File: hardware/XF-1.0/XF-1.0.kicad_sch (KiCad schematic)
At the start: 9 parts

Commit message: modified:   Ferrite Transformer Calculation.xlsx 	modified:   README.md 	deleted:    hardware/XF-1.0/XF-1.0-backups/XF-1.0-2025-07-15_095716.zip 	new file:   hardware/XF-1.0/XF-1.0-backups/XF-1.0-2025-07-15_145509.zip 	new file:   hardware/XF-1.0/XF-1.0-backups/XF-1.0-2025-07-15_150114.zip 	new file:   hardware/XF-1.0/XF-1.0-backups/XF-1.0-2025-07-15_150614.zip 	new file:   hardware/XF-1.0/XF-1.0-backups/XF-1.0-2025-07-15_151503.zip 	new file:   hardware/XF-1.0/XF-1.0-backups/XF-1.0-2025-07-15_152320.zip 	new file:   hardware/XF-1.0/XF-1.0-backups/XF-1.0-2025-07-15_154638.zip 	modified:   hardware/XF-1.0/XF-1.0.kicad_pcb 	modified:   hardware/XF-1.0/XF-1.0.kicad_prl 	modified:   hardware/XF-1.0/XF-1.0.kicad_pro 	modified:   hardware/XF-1.0/XF-1.0.kicad_sch 	modified:   hardware/XF-1.0/_autosave-XF-1.0.kicad_sch 	modified:   hardware/XF-1.0/fp-info-cache
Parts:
- removed C1-2, C1-3: 1nF, Capacitor_THT:C_Rect_L13.0mm_W8.0mm_P10.00mm_FKS3_FKP3_MKS4, symbol Device:C
- removed L1, L2: ~, Transformer_THT:Inductor-EE25, symbol Device:L_Ferrite
- removed TF1: ~, Transformer_THT:EE35-1P-1S-Vertical-2143, symbol Transformer:ER35-1P-1S
- added CN1, CN2: Conn_01x02, Connector_Molex:Molex_KK-396_5273-03A_1x03_P3.96mm_Vertical_2, symbol Connector_Generic:Conn_01x02
- added L1, L2: 29µH, Inductor_THT:L_Radial_Multilayer_D8.0mm_P12.70mm, symbol Device:L
- added XF1: ~, Transformer_THT:Transformer_Toroid_Horizontal_OD40_ID23_H15, symbol Transformer:TRANSF1
- C1: renamed from C1-1; value 1nF -> 2.7nF
- R1: value R_US -> RBTL
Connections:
- net at C3.1: now also C1.2, L2.2
- net at C3.2, R1.2: now also CN2.2 (Pin_2)
- net at C1.1, C2.1: now also L1.2
- net at C2.2, R1.1: now also CN2.1 (Pin_1)
- new net: L1.1, XF1.4
- new net: L2.1, XF1.3
- new net: CN1.1 (Pin_1), XF1.1
- new net: CN1.2 (Pin_2), XF1.2
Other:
- moved on the sheet: C1

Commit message: modified:   Ferrite Transformer Calculation.xlsx 	modified:   README.md 	deleted:    hardware/CTL-1.0/CTL-1.0-backups/CTL-1.0-2025-05-28_203223.zip 	new file:   hardware/CTL-1.0/CTL-1.0-backups/CTL-1.0-2025-07-16_143147.zip 	deleted:    hardware/PS-2.0/PS-2.0-backups/PS-2.0-2025-05-06_105341.zip 	new file:   hardware/PS-2.0/PS-2.0-backups/PS-2.0-2025-07-17_090338.zip 	deleted:    hardware/XF-1.0/#auto_saved_files# 	deleted:    hardware/XF-1.0/XF-1.0-backups/XF-1.0-2025-07-15_145509.zip 	new file:   hardware/XF-1.0/XF-1.0-backups/XF-1.0-2025-07-16_140719.zip 	new file:   hardware/XF-1.0/XF-1.0-backups/XF-1.0-2025-07-17_091914.zip 	new file:   hardware/XF-1.0/XF-1.0-backups/XF-1.0-2025-07-17_092825.zip 	new file:   hardware/XF-1.0/XF-1.0-backups/XF-1.0-2025-07-17_093426.zip 	new file:   hardware/XF-1.0/XF-1.0-backups/XF-1.0-2025-07-17_103845.zip 	new file:   hardware/XF-1.0/XF-1.0-backups/XF-1.0-2025-07-17_105026.zip 	new file:   hardware/XF-1.0/XF-1.0-backups/XF-1.0-2025-07-17_105651.zip 	modified:   hardware/XF-1.0/XF-1.0.kicad_pcb 	modified:   hardware/XF-1.0/XF-1.0.kicad_pro 	modified:   hardware/XF-1.0/XF-1.0.kicad_sch 	deleted:    hardware/XF-1.0/_autosave-XF-1.0.kicad_sch 	modified:   hardware/XF-1.0/fp-info-cache 	modified:   log.md
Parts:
- added C1-1, C1-3, C4-1, C4-2, C4-3: 2.7nF, Capacitor_THT:C_Rect_L13.0mm_W8.0mm_P10.00mm_FKS3_FKP3_MKS4, symbol Device:C
- added C5, C6: 4.7nF, Capacitor_THT:C_Rect_L13.0mm_W8.0mm_P10.00mm_FKS3_FKP3_MKS4, symbol Device:C
- added CN3, CN4: Conn_01x02, Connector_Molex:Molex_KK-396_5273-03A_1x03_P3.96mm_Vertical_2, symbol Connector_Generic:Conn_01x02
- added H1, H2, H3, H4: ~, MountingHole:MountingHole_3mm_Pad, symbol Mechanical:MountingHole_Pad
- added L3, L4: 29µH, Inductor_THT:L_Radial_Multilayer_D8.0mm_P12.70mm, symbol Device:L
- added R2: RBTL, symbol Device:R_US
- added XF2: ~, Transformer_THT:Transformer_Toroid_Horizontal_OD40_ID23_H15, symbol Transformer:TRANSF1
- renumbered C1 to C1-2
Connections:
- net at C3.1, L2.2: now also C1-3.2; no longer C1-2.2
- net at C2.1, L1.2: now also C1-1.1; no longer C1-2.1
- new net: C5.2, CN4.1 (Pin_1), R2.1
- new net: C6.2, CN4.2 (Pin_2), R2.2
- new net: C1-1.2, C1-2.1
- new net: C1-2.2, C1-3.1
- new net: L4.1, XF2.3
- new net: C4-3.2, C6.1, L4.2
- new net: C4-1.1, C5.1, L3.2
- new net: C4-1.2, C4-2.1
- new net: C4-2.2, C4-3.1
- new net: L3.1, XF2.4
- new net: CN3.1 (Pin_1), XF2.1
- new net: CN3.2 (Pin_2), XF2.2

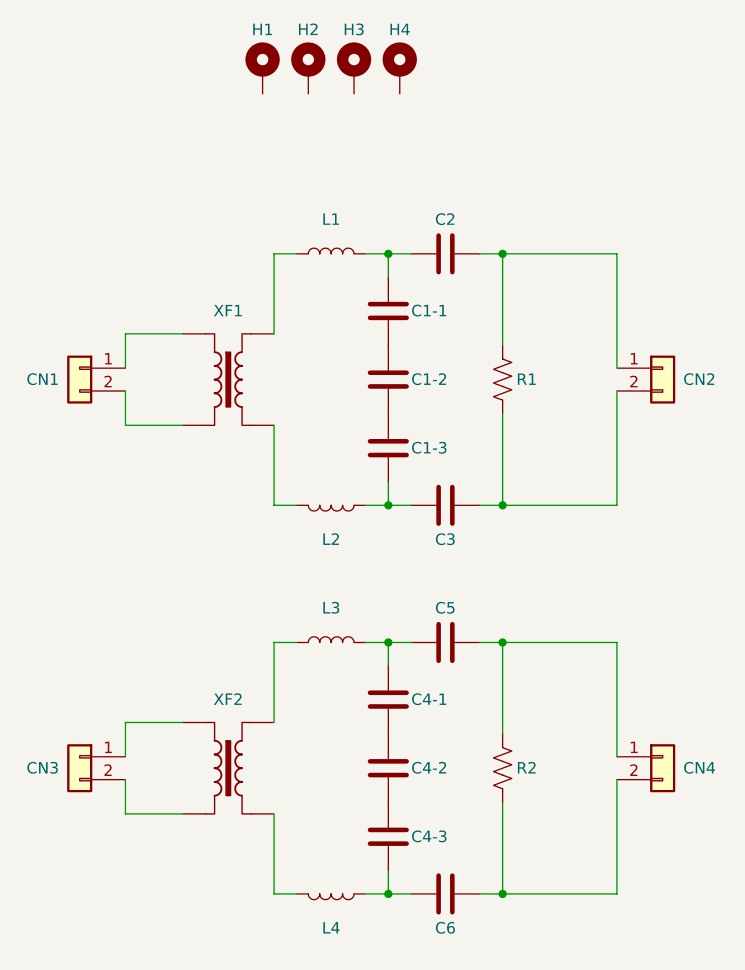
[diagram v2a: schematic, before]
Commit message: deleted:    hardware/PS-2.0/PS-2.0-backups/PS-2.0-2025-05-06_110321.zip 	deleted:    hardware/PS-2.0/PS-2.0-backups/PS-2.0-2025-05-06_111001.zip 	deleted:    hardware/PS-2.0/PS-2.0-backups/PS-2.0-2025-05-06_111519.zip 	deleted:    hardware/PS-2.0/PS-2.0-backups/PS-2.0-2025-05-06_112237.zip 	new file:   hardware/PS-2.0/PS-2.0-backups/PS-2.0-2025-07-17_141237.zip 	new file:   hardware/PS-2.0/PS-2.0-backups/PS-2.0-2025-07-17_142153.zip 	new file:   hardware/PS-2.0/PS-2.0-backups/PS-2.0-2025-07-17_143639.zip 	new file:   hardware/PS-2.0/PS-2.0-backups/PS-2.0-2025-07-17_144647.zip 	deleted:    hardware/XF-1.0/XF-1.0-backups/XF-1.0-2025-07-17_091914.zip 	deleted:    hardware/XF-1.0/XF-1.0-backups/XF-1.0-2025-07-17_092825.zip 	deleted:    hardware/XF-1.0/XF-1.0-backups/XF-1.0-2025-07-17_093426.zip 	deleted:    hardware/XF-1.0/XF-1.0-backups/XF-1.0-2025-07-17_103845.zip 	deleted:    hardware/XF-1.0/XF-1.0-backups/XF-1.0-2025-07-17_105026.zip 	deleted:    hardware/XF-1.0/XF-1.0-backups/XF-1.0-2025-07-17_105651.zip 	new file:   hardware/XF-1.0/XF-1.0-backups/XF-1.0-2025-07-17_144932.zip 	new file:   hardware/XF-1.0/XF-1.0-backups/XF-1.0-2025-07-17_145542.zip 	new file:   hardware/XF-1.0/XF-1.0-backups/XF-1.0-2025-07-17_150101.zip 	new file:   hardware/XF-1.0/XF-1.0-backups/XF-1.0-2025-07-17_150621.zip 	new file:   hardware/XF-1.0/XF-1.0-backups/XF-1.0-2025-07-17_151256.zip 	new file:   hardware/XF-1.0/XF-1.0-backups/XF-1.0-2025-07-17_151907.zip 	modified:   hardware/XF-1.0/XF-1.0.kicad_pcb 	modified:   hardware/XF-1.0/XF-1.0.kicad_pro 	modified:   hardware/XF-1.0/XF-1.0.kicad_sch
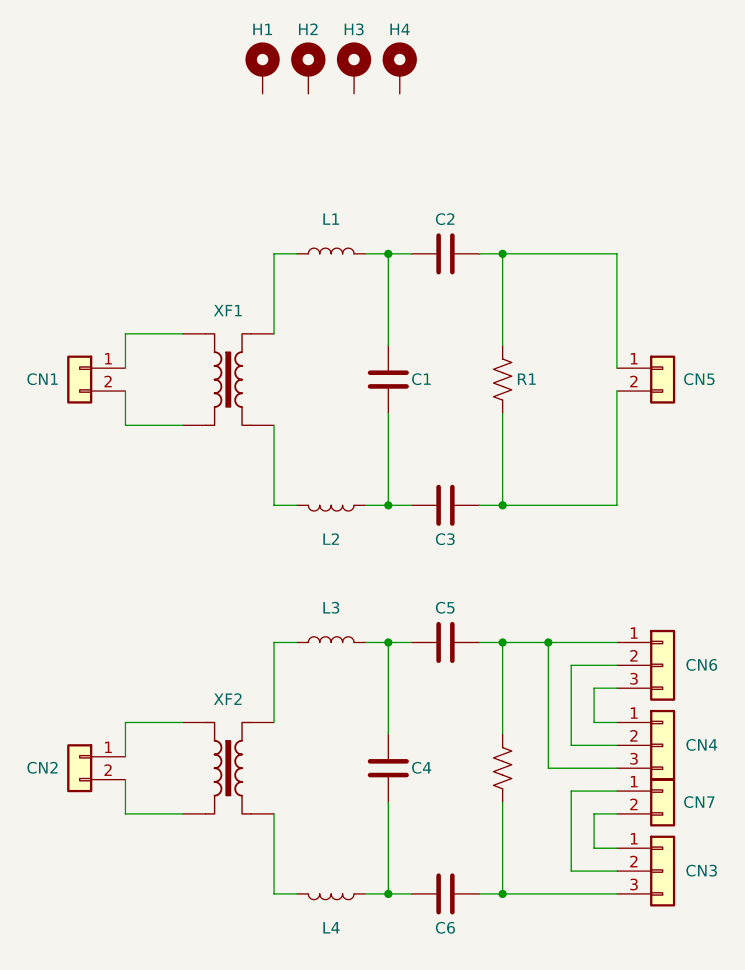
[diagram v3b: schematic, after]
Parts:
- removed C1-1, C1-3, C4-1, C4-3: 2.7nF, Capacitor_THT:C_Rect_L13.0mm_W8.0mm_P10.00mm_FKS3_FKP3_MKS4, symbol Device:C
- removed CN4: Conn_01x02, Connector_Molex:Molex_KK-396_5273-03A_1x03_P3.96mm_Vertical_2, symbol Connector_Generic:Conn_01x02
- added CN3, CN4, CN6: Conn_01x03, Connector_Molex:Molex_KK-396_5273-05A_1x05_P3.96mm_Vertical_2, symbol Connector_Generic:Conn_01x03
- added CN7: Conn_01x02, Connector_Molex:Molex_KK-396_5273-03A_1x03_P3.96mm_Vertical_2, symbol Connector_Generic:Conn_01x02
- renumbered C1-2 to C1, C4-2 to C4, CN3 to CN2, CN2 to CN5
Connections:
- net at C5.2, R2.1: now also CN4.3 (Pin_3), CN6.1 (Pin_1)
- net at C6.2, R2.2: now also CN3.3 (Pin_3)
- net at C3.1, L2.2: now also C1.2
- net at C1.1: now also C2.1, L1.2
- net at C6.1, L4.2: now also C4.2
- net at C5.1, L3.2: now also C4.1
- new net: CN3.2 (Pin_2), CN7.1 (Pin_1)
- new net: CN3.1 (Pin_1), CN7.2 (Pin_2)
- new net: CN4.1 (Pin_1), CN6.3 (Pin_3)
- new net: CN4.2 (Pin_2), CN6.2 (Pin_2)

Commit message: modified:   README.md 	deleted:    hardware/CTL-1.0/CTL-1.0-backups/CTL-1.0-2025-05-28_203806.zip 	deleted:    hardware/CTL-1.0/CTL-1.0-backups/CTL-1.0-2025-05-28_204313.zip 	deleted:    hardware/CTL-1.0/CTL-1.0-backups/CTL-1.0-2025-05-30_173028.zip 	deleted:    hardware/CTL-1.0/CTL-1.0-backups/CTL-1.0-2025-05-30_174116.zip 	deleted:    hardware/CTL-1.0/CTL-1.0-backups/CTL-1.0-2025-05-30_175122.zip 	new file:   hardware/CTL-1.0/CTL-1.0-backups/CTL-1.0-2025-07-24_151142.zip 	new file:   hardware/CTL-1.0/CTL-1.0-backups/CTL-1.0-2025-07-24_172002.zip 	new file:   hardware/CTL-1.0/CTL-1.0-backups/CTL-1.0-2025-07-25_175122.zip 	new file:   hardware/CTL-1.0/CTL-1.0-backups/CTL-1.0-2025-07-26_120011.zip 	new file:   hardware/CTL-1.0/CTL-1.0-backups/CTL-1.0-2025-07-26_120808.zip 	modified:   hardware/CTL-1.0/CTL-1.0.kicad_pcb 	modified:   hardware/CTL-1.0/CTL-1.0.kicad_pro 	new file:   hardware/CTL-1.0/CTL-1.0.step 	deleted:    hardware/MSD-1.0/MSD-1.0-backups/MSD-1.0-2025-04-11_111943.zip 	deleted:    hardware/MSD-1.0/MSD-1.0-backups/MSD-1.0-2025-04-11_113401.zip 	new file:   hardware/MSD-1.0/MSD-1.0-backups/MSD-1.0-2025-07-25_163151.zip 	new file:   hardware/MSD-1.0/MSD-1.0-backups/MSD-1.0-2025-07-25_171843.zip 	modified:   hardware/MSD-1.0/MSD-1.0.kicad_pcb 	modified:   hardware/MSD-1.0/MSD-1.0.step 	new file:   hardware/MSD-1.1/MSD-1.1-backups/MSD-1.1-2025-07-24_151252.zip 	new file:   hardware/MSD-1.1/MSD-1.1-backups/MSD-1.1-2025-07-25_152939.zip 	new file:   hardware/MSD-1.1/MSD-1.1-backups/MSD-1.1-2025-07-25_162346.zip 	new file:   hardware/MSD-1.1/MSD-1.1-backups/MSD-1.1-2025-07-25_162917.zip 	modified:   hardware/MSD-1.1/MSD-1.1.kicad_pcb 	modified:   hardware/MSD-1.1/MSD-1.1.step 	modified:   hardware/MSD-1.1/fp-info-cache 	new file:   hardware/MSD-2.0/MSD-2.0-backups/MSD-2.0-2025-07-24_151230.zip 	deleted:    hardware/PS-2.0/PS-2.0-backups/PS-2.0-2025-05-07_010425.zip 	deleted:    hardware/PS-2.0/PS-2.0-backups/PS-2.0-2025-05-09_084820.zip 	deleted:    hardware/P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
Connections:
- net at C6.2, R2.2: now also CN3.1 (Pin_1); no longer CN3.3 (Pin_3)
- net at CN7.1 (Pin_1): now also CN3.3 (Pin_3); no longer CN3.2 (Pin_2)
- net at CN7.2 (Pin_2): now also CN3.2 (Pin_2); no longer CN3.1 (Pin_1)
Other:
- moved on the sheet: CN3
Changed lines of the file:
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@@
+	)
+	(junction
+		(at 149.86 87.63)
+		(diameter 0)
+		(color 0 0 0 0)
+	)
+	(junction
+		(at 162.56 102.87)
+		(diameter 0)
+		(color 0 0 0 0)
+	)
+	(junction
+		(at 162.56 59.69)
+		(diameter 0)
+		(color 0 0 0 0)
 	)
 	(junction
@@
 		(color 0 0 0 0)
 	)
-	(junction
-		(at 149.86 87.63)
-		(diameter 0)
-		(color 0 0 0 0)
-	)
-	(junction
-		(at 162.56 102.87)
-		(diameter 0)
-		(color 0 0 0 0)
-	)
-	(junction
-		(at 162.56 59.69)
-		(diameter 0)
-		(color 0 0 0 0)
-	)
 	(wire
 		(pts
@@
 	(wire
 		(pts
+			(xy 175.26 133.35) (xy 172.72 133.35)
+		)
+		(stroke
+			(width 0)
+			(type default)
+		)
+	)
+	(wire
+		(pts
 			(xy 160.02 59.69) (xy 162.56 59.69)
 		)
@@
 	(wire
 		(pts
-			(xy 172.72 121.92) (xy 172.72 125.73)
-		)
-		(stroke
-			(width 0)
-			(type default)
-		)
-	)
-	(wire
-		(pts
 			(xy 167.64 102.87) (xy 175.26 102.87)
 		)
@@
 	(wire
 		(pts
-			(xy 170.18 119.38) (xy 170.18 128.27)
-		)
-		(stroke
-			(width 0)
-			(type default)
-		)
-	)
-	(wire
-		(pts
 			(xy 120.65 78.74) (xy 127 78.74)
 		)
@@
 	(wire
 		(pts
+			(xy 172.72 121.92) (xy 172.72 133.35)
+		)
+		(stroke
+			(width 0)
+			(type default)
+		)
+	)
+	(wire
+		(pts
 			(xy 137.16 130.81) (xy 139.7 130.81)
 		)
@@
 	(wire
 		(pts
+			(xy 170.18 119.38) (xy 170.18 135.89)
+		)
+		(stroke
+			(width 0)
+			(type default)
+		)
+	)
+	(wire
+		(pts
 			(xy 137.16 121.92) (xy 137.16 130.81)
 		)
@@
 	(wire
 		(pts
+			(xy 162.56 130.81) (xy 175.26 130.81)
+		)
+		(stroke
+			(width 0)
+			(type default)
+		)
+	)
+	(wire
+		(pts
 			(xy 120.65 74.93) (xy 120.65 78.74)
 		)
@@
 	(wire
 		(pts
-			(xy 162.56 130.81) (xy 175.26 130.81)
-		)
-		(stroke
-			(width 0)
-			(type default)
-		)
-	)
-	(wire
-		(pts
 			(xy 162.56 77.47) (xy 162.56 87.63)
 		)
@@
 	(wire
 		(pts
-			(xy 172.72 125.73) (xy 175.26 125.73)
-		)
-		(stroke
-			(width 0)
-			(type default)
-		)
-	)
-	(wire
-		(pts
 			(xy 162.56 87.63) (xy 175.26 87.63)
 		)
@@
 	(wire
 		(pts
-			(xy 170.18 128.27) (xy 175.26 128.27)
-		)
-		(stroke
-			(width 0)
-			(type default)
-		)
-	)
-	(wire
-		(pts
 			(xy 160.02 130.81) (xy 162.56 130.81)
 		)
@@
 		(pts
 			(xy 175.26 111.76) (xy 172.72 111.76)
+		)
+		(stroke
+			(width 0)
+			(type default)
+		)
+	)
+	(wire
+		(pts
+			(xy 175.26 135.89) (xy 170.18 135.89)
 		)
 		(stroke
@@
 	(symbol
 		(lib_id "Connector_Generic:Conn_01x03")
-		(at 180.34 128.27 0)
+		(at 180.34 133.35 0)
 		(unit 1)
 		(exclude_from_sim no)
@@
 		(dnp no)
 		(property "Reference" "CN3"
-			(at 182.88 128.27 0)
+			(at 182.88 133.35 0)
 			(effects
 				(font
@@
 		)
 		(property "Value" "Conn_01x03"
-			(at 182.88 129.5399 0)
+			(at 182.88 134.6199 0)
 			(effects
 				(font
@@
 		)
 		(property "Footprint" "Connector_Molex:Molex_KK-396_5273-05A_1x05_P3.96mm_Vertical_2"
-			(at 180.34 128.27 0)
+			(at 180.34 133.35 0)
 			(effects
 				(font
@@
 		)
 		(property "Datasheet" "~"
-			(at 180.34 128.27 0)
+			(at 180.34 133.35 0)
 			(effects
 				(font
@@
 		)
 		(property "Description" "Generic connector, single row, 01x03, script generated (kicad-library-utils/schlib/autogen/connector/)"
-			(at 180.34 128.27 0)
-			(effects
-				(font
+			(at 180.34 133.35 0)
+			(effects
+				(font

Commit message: modified:   .DS_Store 	new file:   hardware/.~Request PO 20250807.xlsx 	new file:   hardware/CTL-3.0/.~BoM.xlsx 	modified:   hardware/CTL-3.0/BoM.xlsx 	deleted:    hardware/PS-2.0/PS-2.0-backups/PS-2.0-2025-07-26_112315.zip 	deleted:    hardware/PS-2.0/PS-2.0-backups/PS-2.0-2025-07-26_113619.zip 	deleted:    hardware/PS-2.0/PS-2.0-backups/PS-2.0-2025-07-26_114654.zip 	deleted:    hardware/PS-2.0/PS-2.0-backups/PS-2.0-2025-08-06_121001.zip 	new file:   hardware/PS-2.0/PS-2.0-backups/PS-2.0-2025-08-07_142024.zip 	new file:   hardware/PS-2.0/PS-2.0-backups/PS-2.0-2025-08-07_143133.zip 	new file:   hardware/PS-2.0/PS-2.0-backups/PS-2.0-2025-08-07_145326.zip 	new file:   hardware/PS-2.0/PS-2.0-backups/PS-2.0-2025-08-07_160132.zip 	new file:   hardware/PS-2.0/PS-2.0-backups/PS-2.0-2025-08-07_161316.zip 	new file:   hardware/PS-2.0/_autosave-PS-2.0.kicad_pcb 	new file:   hardware/PS-2.0/~_autosave-PS-2.0.kicad_pcb.lck 	new file:   hardware/Request PO 20250807 1029.xlsx 	deleted:    hardware/XF-1.0/XF-1.0-backups/XF-1.0-2025-07-15_152320.zip 	deleted:    hardware/XF-1.0/XF-1.0-backups/XF-1.0-2025-07-15_154638.zip 	deleted:    hardware/XF-1.0/XF-1.0-backups/XF-1.0-2025-07-16_140719.zip 	deleted:    hardware/XF-1.0/XF-1.0-backups/XF-1.0-2025-07-17_145542.zip 	deleted:    hardware/XF-1.0/XF-1.0-backups/XF-1.0-2025-07-17_150101.zip 	deleted:    hardware/XF-1.0/XF-1.0-backups/XF-1.0-2025-07-17_150621.zip 	deleted:    hardware/XF-1.0/XF-1.0-backups/XF-1.0-2025-07-17_151256.zip 	new file:   hardware/XF-1.0/XF-1.0-backups/XF-1.0-2025-08-07_145812.zip 	new file:   hardware/XF-1.0/XF-1.0-backups/XF-1.0-2025-08-07_150444.zip 	new file:   hardware/XF-1.0/XF-1.0-backups/XF-1.0-2025-08-07_151358.zip 	new file:   hardware/XF-1.0/XF-1.0-backups/XF-1.0-2025-08-07_152043.zip 	new file:   hardware/XF-1.0/XF-1.0-backups/XF-1.0-2025-08-07_153427.zip 	new file:   hardware/XF-1.0/XF-1.0-backups/XF-1.0-2025-08-07_155906.zip 	modified:   hardware/XF-1.0/XF-1.0.kicad_pcb 	modified:   hardware/XF-1.0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
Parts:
- C1, C4: footprint Capacitor_THT:C_Rect_L13.0mm_W8.0mm_P10.00mm_FKS3_FKP3_MKS4 -> Capacitor_THT:C_Axial_L12.0mm_D6.5mm_P20.00mm_Horizontal
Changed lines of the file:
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@@
 			)
 		)
-		(property "Footprint" "Capacitor_THT:C_Rect_L13.0mm_W8.0mm_P10.00mm_FKS3_FKP3_MKS4"
+		(property "Footprint" "Capacitor_THT:C_Axial_L12.0mm_D6.5mm_P20.00mm_Horizontal"
 			(at 150.8252 77.47 0)
 			(effects
@@
 			)
 		)
-		(property "Footprint" "Capacitor_THT:C_Rect_L13.0mm_W8.0mm_P10.00mm_FKS3_FKP3_MKS4"
+		(property "Footprint" "Capacitor_THT:C_Axial_L12.0mm_D6.5mm_P20.00mm_Horizontal"
 			(at 150.8252 120.65 0)
 			(effects
